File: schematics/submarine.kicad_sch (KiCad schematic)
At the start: 18 parts, among them M1 Motor_DC, M2 Motor_Servo, M3 Motor_Servo, Q1 NMOS, Q2 NMOS, Q3 NMOS, Q4 NMOS, U2 3MP SPI Camera

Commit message: schematic
added temp sensor, startet work on new motor circut, changes to handcontroller
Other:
- sheet Untitled Sheet renamed handControler
- removed sheet camera
- sheet handControler: file untitled.kicad_sch -> handControler.kicad_sch
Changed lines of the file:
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@@
-    (instances
-      (project "submarine"
-        (path "/5a0570be-4b9a-4522-b102-633fe53e4e72" (page "3"))
-      )
-    )
-  )
-  (sheet (at 250.19 119.38) (size 16.51 13.97) (fields_autoplaced)
-    (stroke (width 0.1524) (type solid))
-    (fill (color 0 0 0 0.0000))
-    (property "Sheetname" "camera" (at 250.19 118.6684 0)
-      (effects (font (size 1.27 1.27)) (justify left bottom))
-    )
-    (property "Sheetfile" "cameraSub.kicad_sch" (at 250.19 133.9346 0)
-      (effects (font (size 1.27 1.27)) (justify left top))
-    )
     (instances
       (project "submarine"
@@
     (stroke (width 0.1524) (type solid))
     (fill (color 0 0 0 0.0000))
-    (property "Sheetname" "Untitled Sheet" (at 236.22 135.1784 0)
+    (property "Sheetname" "handControler" (at 236.22 135.1784 0)
       (effects (font (size 1.27 1.27)) (justify left bottom) hide)
     )
-    (property "Sheetfile" "untitled.kicad_sch" (at 236.22 166.9546 0)
+    (property "Sheetfile" "handControler.kicad_sch" (at 236.22 166.9546 0)
       (effects (font (size 1.27 1.27)) (justify left top))
     )
     (instances
       (project "submarine"
-        (path "/5a0570be-4b9a-4522-b102-633fe53e4e72" (page "2"))
+        (path "/5a0570be-4b9a-4522-b102-633fe53e4e72" (page "3"))
       )
     )
@@
     (instances
       (project "submarine"
-        (path "/5a0570be-4b9a-4522-b102-633fe53e4e72" (page "5"))
+        (path "/5a0570be-4b9a-4522-b102-633fe53e4e72" (page "2"))
       )
     )
   )
   (sheet_instances
-    (path "/" (page "1"))
+    (path "/" (page "2"))
   )
 )

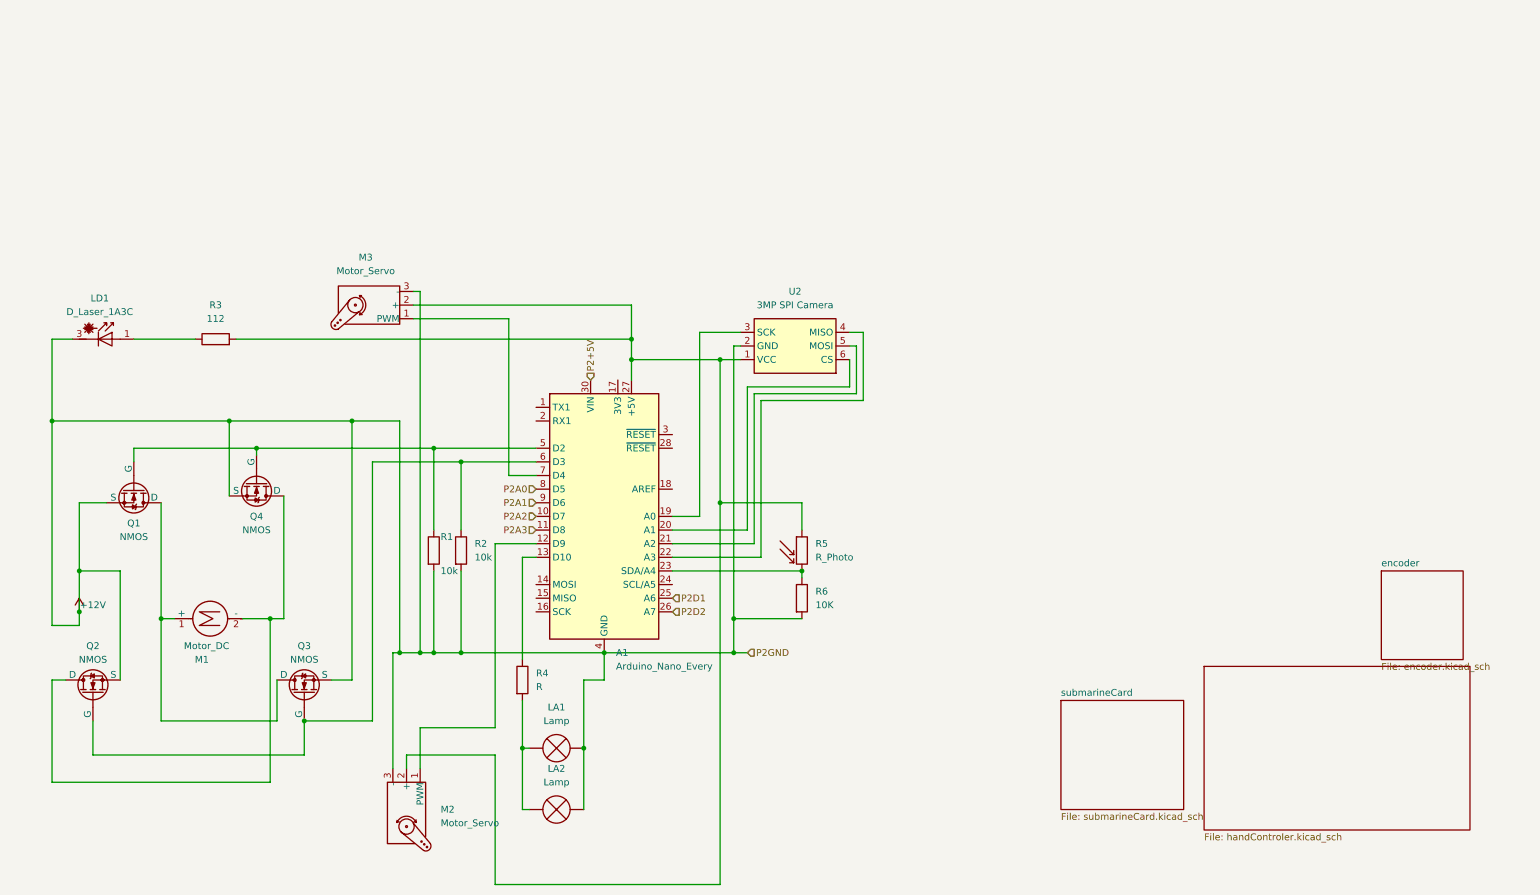
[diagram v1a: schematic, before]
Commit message: added motorCard
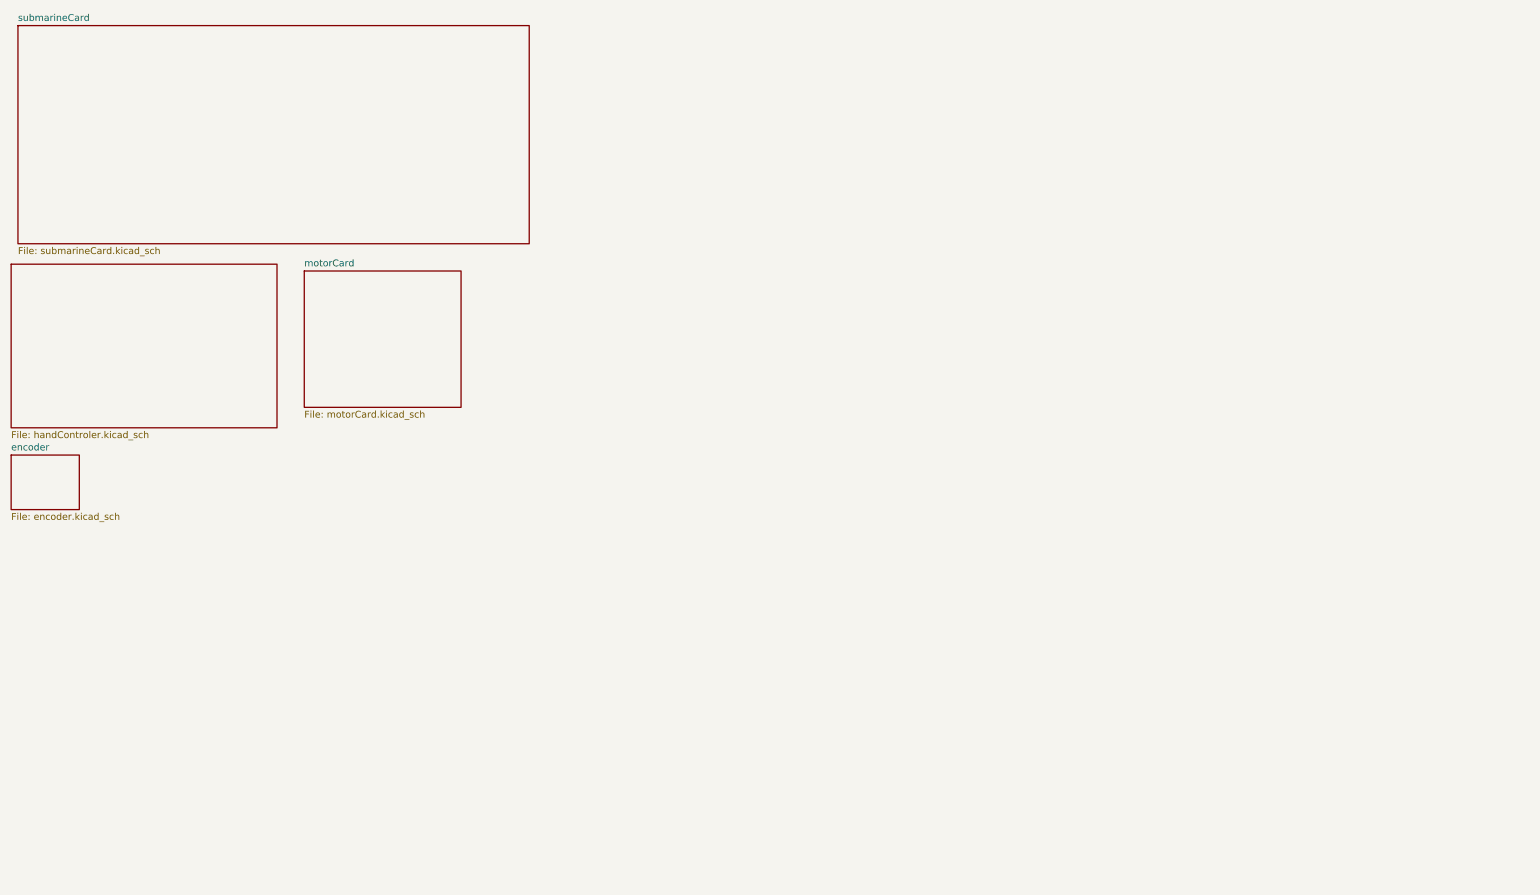
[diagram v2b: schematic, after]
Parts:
- removed A1: Arduino_Nano_Every, Module:Arduino_Nano, symbol MCU_Module:Arduino_Nano_Every
- removed LA1, LA2: Lamp, symbol Device:Lamp
- removed LD1: D_Laser_1A3C, symbol Device:D_Laser_1A3C
- removed M1: Motor_DC, symbol Motor:Motor_DC
- removed M2, M3: Motor_Servo, symbol Motor:Motor_Servo
- removed Q1, Q2, Q3, Q4: NMOS, symbol Simulation_SPICE:NMOS
- removed R1, R2: 10k, symbol Device:R
- removed R3: 112, symbol Device:R
- removed R4: R, symbol Device:R
- removed R5: R_Photo, symbol Device:R_Photo
- removed R6: 10K, symbol Device:R
- removed U2: 3MP SPI Camera, Package_TO_SOT_SMD:SOT-353_SC-70-5, symbol Sensor:3MP_SPI_Camera
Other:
- added sheet motorCard (motorCard.kicad_sch)

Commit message: new motor
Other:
- removed sheet motorCard
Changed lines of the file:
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@@
-    )
-  )
-  (sheet (at 68.58 62.23) (size 29.21 25.4) (fields_autoplaced)
-    (stroke (width 0.1524) (type solid))
-    (fill (color 0 0 0 0.0000))
-    (property "Sheetname" "motorCard" (at 68.58 61.5184 0)
-      (effects (font (size 1.27 1.27)) (justify left bottom))
-    )
-    (property "Sheetfile" "motorCard.kicad_sch" (at 68.58 88.2146 0)
-      (effects (font (size 1.27 1.27)) (justify left top))
-    )
-    (instances
-      (project "submarine"
-        (path "/5a0570be-4b9a-4522-b102-633fe53e4e72" (page "5"))
-      )
     )
   )
